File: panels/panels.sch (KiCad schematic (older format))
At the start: 13 parts, among them J1 Barrel_Jack_Switch, J2 Barrel_Jack_Switch, J3 Barrel_Jack_Switch, J4 Barrel_Jack_Switch, J5 XLR3

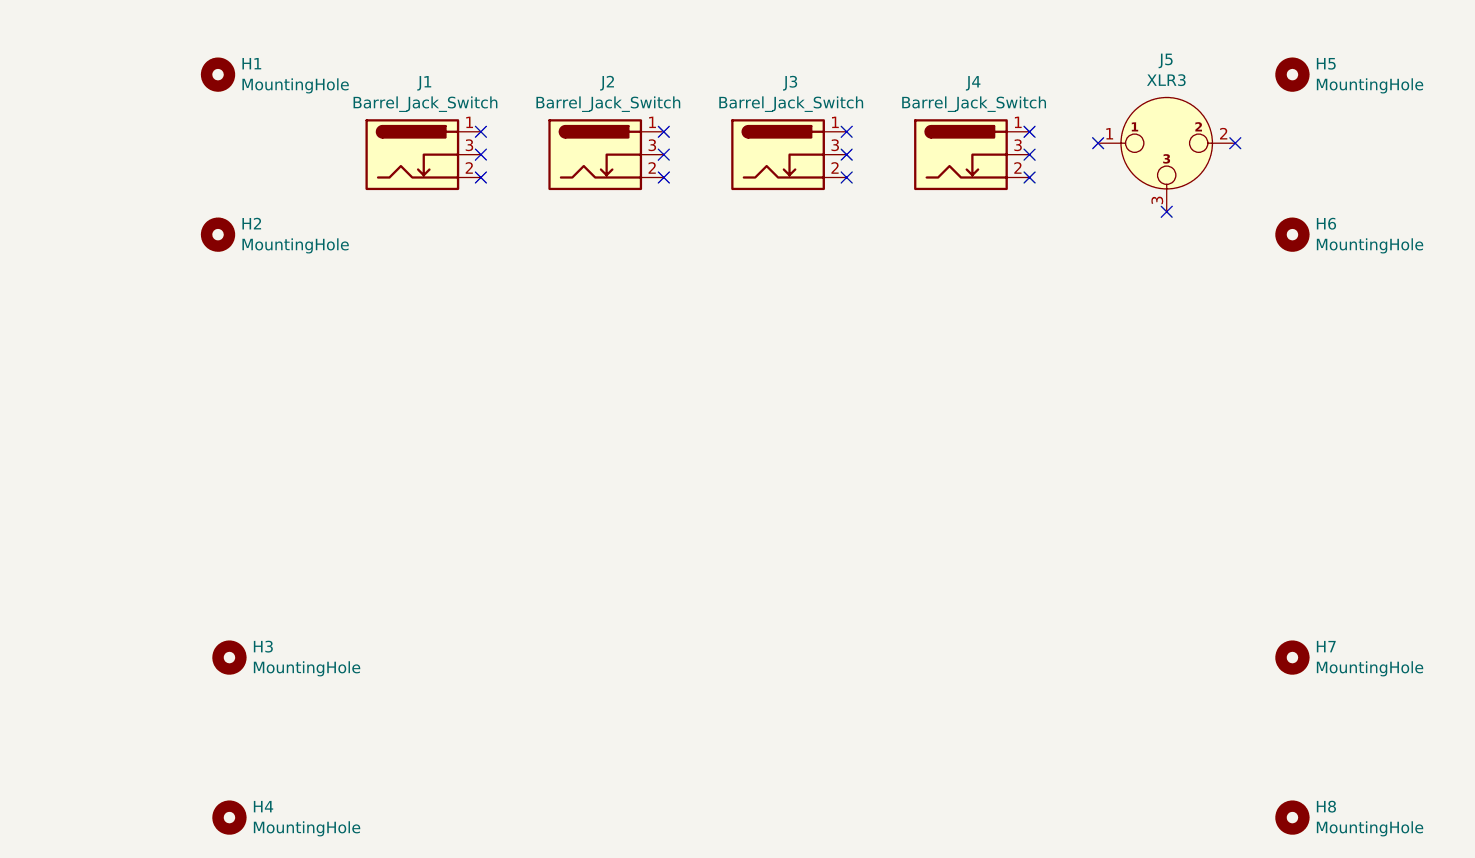
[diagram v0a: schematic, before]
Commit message: Update panels with custom footprints
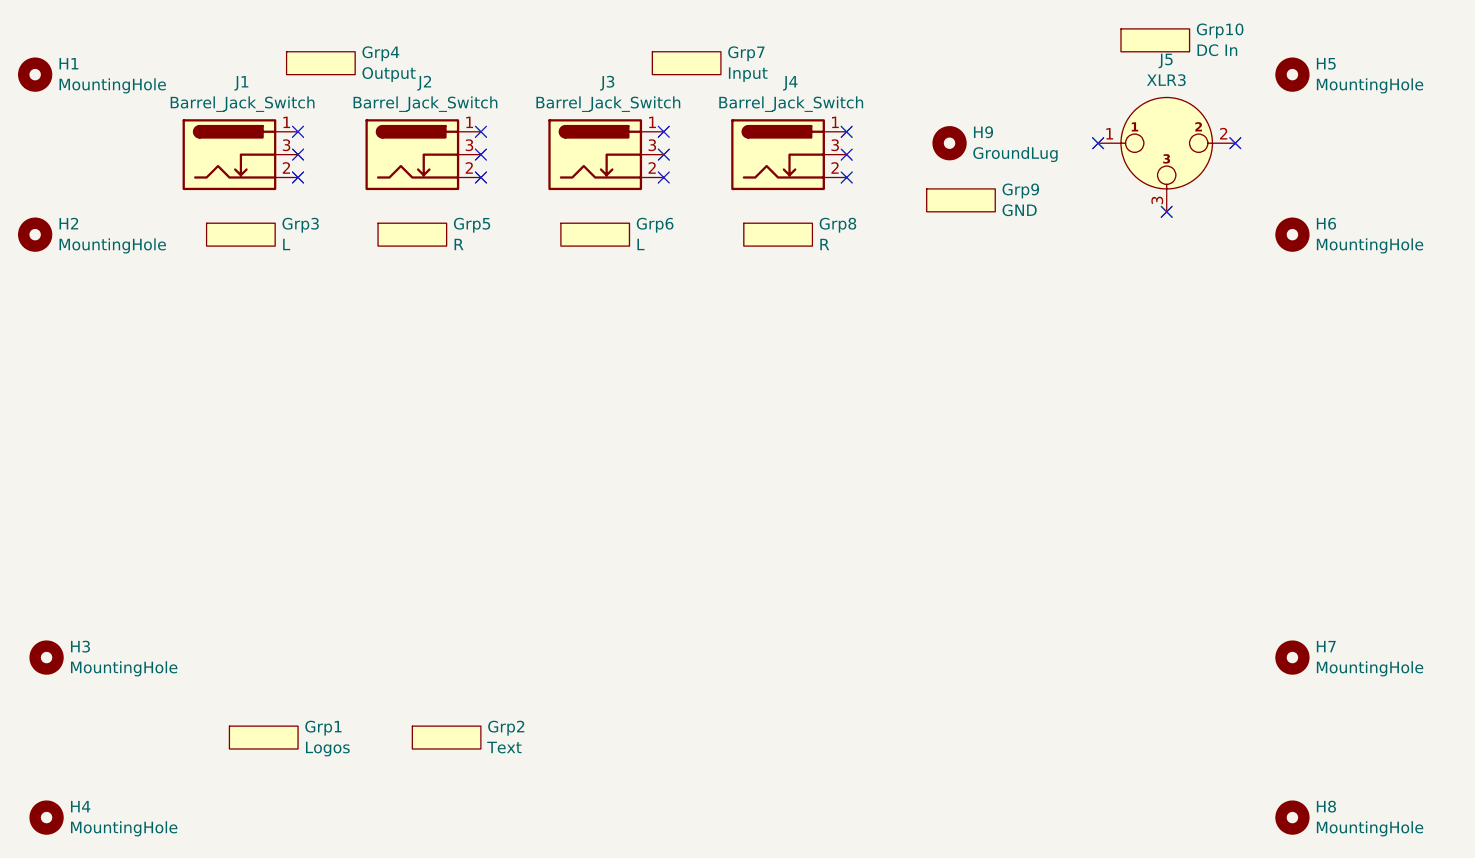
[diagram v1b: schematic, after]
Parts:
- added Grp1: Logos, actidamp-mk4-smd:FP_Logo, symbol actidamp:Graphic
- added Grp10: DC In, actidamp-mk4-smd:BP_text_DC_In, symbol actidamp:Graphic
- added Grp2: Text, actidamp-mk4-smd:FP_text, symbol actidamp:Graphic
- added Grp3, Grp6: L, actidamp-mk4-smd:BP_text_L, symbol actidamp:Graphic
- added Grp4: Output, actidamp-mk4-smd:BP_text_output, symbol actidamp:Graphic
- added Grp5, Grp8: R, actidamp-mk4-smd:BP_text_R, symbol actidamp:Graphic
- added Grp7: Input, actidamp-mk4-smd:BP_text_input, symbol actidamp:Graphic
- added Grp9: GND, actidamp-mk4-smd:BP_text_GND, symbol actidamp:Graphic
- added H9: GroundLug, MountingHole:MountingHole_4.3mm_M4, symbol Mechanical:MountingHole
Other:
- moved on the sheet: H1, H2, H3, H4, J1, J2, J3, J4
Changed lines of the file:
@@
 L Mechanical:MountingHole H1
 U 1 1 5DB88982
-P 2650 1900
-F 0 "H1" H 2750 1946 50  0000 L CNN
-F 1 "MountingHole" H 2750 1855 50  0000 L CNN
-F 2 "MountingHole:MountingHole_3.5mm" H 2650 1900 50  0001 C CNN
-F 3 "~" H 2650 1900 50  0001 C CNN
-	1    2650 1900
+P 1850 1900
+F 0 "H1" H 1950 1946 50  0000 L CNN
+F 1 "MountingHole" H 1950 1855 50  0000 L CNN
+F 2 "MountingHole:MountingHole_3.5mm" H 1850 1900 50  0001 C CNN
+F 3 "~" H 1850 1900 50  0001 C CNN
+	1    1850 1900
 	1    0    0    -1
 $EndComp
@@
 L Mechanical:MountingHole H2
 U 1 1 5DB88E12
-P 2650 2600
-F 0 "H2" H 2750 2646 50  0000 L CNN
-F 1 "MountingHole" H 2750 2555 50  0000 L CNN
-F 2 "MountingHole:MountingHole_3.5mm" H 2650 2600 50  0001 C CNN
-F 3 "~" H 2650 2600 50  0001 C CNN
-	1    2650 2600
+P 1850 2600
+F 0 "H2" H 1950 2646 50  0000 L CNN
+F 1 "MountingHole" H 1950 2555 50  0000 L CNN
+F 2 "MountingHole:MountingHole_3.5mm" H 1850 2600 50  0001 C CNN
+F 3 "~" H 1850 2600 50  0001 C CNN
+	1    1850 2600
 	1    0    0    -1
 $EndComp
@@
 L Mechanical:MountingHole H3
 U 1 1 5DB8B1F4
-P 2700 4450
-F 0 "H3" H 2800 4496 50  0000 L CNN
-F 1 "MountingHole" H 2800 4405 50  0000 L CNN
-F 2 "MountingHole:MountingHole_3.5mm" H 2700 4450 50  0001 C CNN
-F 3 "~" H 2700 4450 50  0001 C CNN
-	1    2700 4450
+P 1900 4450
+F 0 "H3" H 2000 4496 50  0000 L CNN
+F 1 "MountingHole" H 2000 4405 50  0000 L CNN
+F 2 "MountingHole:MountingHole_3.5mm" H 1900 4450 50  0001 C CNN
+F 3 "~" H 1900 4450 50  0001 C CNN
+	1    1900 4450
 	1    0    0    -1
 $EndComp
@@
 L Mechanical:MountingHole H4
 U 1 1 5DB8B208
-P 2700 5150
-F 0 "H4" H 2800 5196 50  0000 L CNN
-F 1 "MountingHole" H 2800 5105 50  0000 L CNN
-F 2 "MountingHole:MountingHole_3.5mm" H 2700 5150 50  0001 C CNN
-F 3 "~" H 2700 5150 50  0001 C CNN
-	1    2700 5150
+P 1900 5150
+F 0 "H4" H 2000 5196 50  0000 L CNN
+F 1 "MountingHole" H 2000 5105 50  0000 L CNN
+F 2 "MountingHole:MountingHole_3.5mm" H 1900 5150 50  0001 C CNN
+F 3 "~" H 1900 5150 50  0001 C CNN
+	1    1900 5150
 	1    0    0    -1
 $EndComp
@@
 L Connector:Barrel_Jack_Switch J1
 U 1 1 5DB95C23
+P 2700 2250
+F 0 "J1" H 2757 2567 50  0000 C CNN
+F 1 "Barrel_Jack_Switch" H 2757 2476 50  0000 C CNN
+F 2 "actidamp-mk4-smd:RCA_x1_PJRAN1X1U_FP" H 2750 2210 50  0001 C CNN
+F 3 "~" H 2750 2210 50  0001 C CNN
+	1    2700 2250
+	1    0    0    -1
+$EndComp
+$Comp
+L Connector:Barrel_Jack_Switch J2
+U 1 1 5DB96D2B
 P 3500 2250
-F 0 "J1" H 3557 2567 50  0000 C CNN
+F 0 "J2" H 3557 2567 50  0000 C CNN
 F 1 "Barrel_Jack_Switch" H 3557 2476 50  0000 C CNN
 F 2 "actidamp-mk4-smd:RCA_x1_PJRAN1X1U_FP" H 3550 2210 50  0001 C CNN
@@
 $EndComp
 $Comp
-L Connector:Barrel_Jack_Switch J2
-U 1 1 5DB96D2B
+L Connector:Barrel_Jack_Switch J3
+U 1 1 5DB97302
 P 4300 2250
-F 0 "J2" H 4357 2567 50  0000 C CNN
+F 0 "J3" H 4357 2567 50  0000 C CNN
 F 1 "Barrel_Jack_Switch" H 4357 2476 50  0000 C CNN
 F 2 "actidamp-mk4-smd:RCA_x1_PJRAN1X1U_FP" H 4350 2210 50  0001 C CNN
@@
 $EndComp
 $Comp
-L Connector:Barrel_Jack_Switch J3
-U 1 1 5DB97302
+L Connector:Barrel_Jack_Switch J4
+U 1 1 5DB977A2
 P 5100 2250
-F 0 "J3" H 5157 2567 50  0000 C CNN
+F 0 "J4" H 5157 2567 50  0000 C CNN
 F 1 "Barrel_Jack_Switch" H 5157 2476 50  0000 C CNN
 F 2 "actidamp-mk4-smd:RCA_x1_PJRAN1X1U_FP" H 5150 2210 50  0001 C CNN
 F 3 "~" H 5150 2210 50  0001 C CNN
 	1    5100 2250
-	1    0    0    -1
-$EndComp
-$Comp
-L Connector:Barrel_Jack_Switch J4
-U 1 1 5DB977A2
-P 5900 2250
-F 0 "J4" H 5957 2567 50  0000 C CNN
-F 1 "Barrel_Jack_Switch" H 5957 2476 50  0000 C CNN
-F 2 "actidamp-mk4-smd:RCA_x1_PJRAN1X1U_FP" H 5950 2210 50  0001 C CNN
-F 3 "~" H 5950 2210 50  0001 C CNN
-	1    5900 2250
 	1    0    0    -1
 $EndComp
@@
 	1    0    0    -1
 $EndComp
+NoConn ~ 3000 2150
+NoConn ~ 3000 2250
+NoConn ~ 3000 2350
 NoConn ~ 3800 2150
 NoConn ~ 3800 2250
@@
 NoConn ~ 5400 2250
 NoConn ~ 5400 2350
-NoConn ~ 6200 2150
-NoConn ~ 6200 2250
-NoConn ~ 6200 2350
 NoConn ~ 6500 2200
 NoConn ~ 6800 2500
 NoConn ~ 7100 2200
+$Comp
+L Mechanical:MountingHole H9
+U 1 1 5DBA5314
+P 5850 2200
+F 0 "H9" H 5950 2246 50  0000 L CNN
+F 1 "GroundLug" H 5950 2155 50  0000 L CNN
+F 2 "MountingHole:MountingHole_4.3mm_M4" H 5850 2200 50  0001 C CNN
+F 3 "~" H 5850 2200 50  0001 C CNN
+	1    5850 2200
+	1    0    0    -1
+$EndComp
+$Comp
+L actidamp:Graphic Grp1
+U 1 1 5DC0A211
+P 2850 4800
+F 0 "Grp1" H 3028 4846 50  0000 L CNN
+F 1 "Logos" H 3028 4755 50  0000 L CNN
+F 2 "actidamp-mk4-smd:FP_Logo" H 2850 4750 50  0001 C CNN
+F 3 "" H 2850 4750 50  0001 C CNN
+	1    2850 4800
+	1    0    0    -1
+$EndComp
+$Comp
+L actidamp:Graphic Grp2
+U 1 1 5DC0A606
+P 3650 4800
+F 0 "Grp2" H 3828 4846 50  0000 L CNN
+F 1 "Text" H 3828 4755 50  0000 L CNN
+F 2 "actidamp-mk4-smd:FP_text" H 3650 4750 50  0001 C CNN
+F 3 "" H 3650 4750 50  0001 C CNN
+	1    3650 4800
+	1    0    0    -1
+$EndComp
+$Comp
+L actidamp:Graphic Grp4
+U 1 1 5DC0FA5B
+P 3100 1850
+F 0 "Grp4" H 3278 1896 50  0000 L CNN
+F 1 "Output" H 3278 1805 50  0000 L CNN
+F 2 "actidamp-mk4-smd:BP_text_output" H 3100 1800 50  0001 C CNN
+F 3 "" H 3100 1800 50  0001 C CNN
+	1    3100 1850
+	1    0    0    -1
+$EndComp
+$Comp
+L actidamp:Graphic Grp7
+U 1 1 5DC0FD71
+P 4700 1850
+F 0 "Grp7" H 4878 1896 50  0000 L CNN
+F 1 "Input" H 4878 1805 50  0000 L CNN
+F 2 "actidamp-mk4-smd:BP_text_input" H 4700 1800 50  0001 C CNN
+F 3 "" H 4700 1800 50  0001 C CNN
+	1    4700 1850
+	1    0    0    -1
+$EndComp
+$Comp
+L actidamp:Graphic Grp3
+U 1 1 5DC10052
+P 2750 2600
+F 0 "Grp3" H 2928 2646 50  0000 L CNN
+F 1 "L" H 2928 2555 50  0000 L CNN
+F 2 "actidamp-mk4-smd:BP_text_L" H 2750 2550 50  0001 C CNN
+F 3 "" H 2750 2550 50  0001 C CNN
+	1    2750 2600
+	1    0    0    -1
+$EndComp
+$Comp
+L actidamp:Graphic Grp5
+U 1 1 5DC10302
+P 3500 2600
+F 0 "Grp5" H 3678 2646 50  0000 L CNN
+F 1 "R" H 3678 2555 50  0000 L CNN
+F 2 "actidamp-mk4-smd:BP_text_R" H 3500 2550 50  0001 C CNN
+F 3 "" H 3500 2550 50  0001 C CNN
+	1    3500 2600
+	1    0    0    -1
+$EndComp
+$Comp
+L actidamp:Graphic Grp6
+U 1 1 5DC1052B
+P 4300 2600
+F 0 "Grp6" H 4478 2646 50  0000 L CNN
+F 1 "L" H 4478 2555 50  0000 L CNN
+F 2 "actidamp-mk4-smd:BP_text_L" H 4300 2550 50  0001 C CNN
+F 3 "" H 4300 2550 50  0001 C CNN
+	1    4300 2600
+	1    0    0    -1
+$EndComp
+$Comp
+L actidamp:Graphic Grp8
+U 1 1 5DC10681
+P 5100 2600
+F 0 "Grp8" H 5278 2646 50  0000 L CNN
+F 1 "R" H 5278 2555 50  0000 L CNN
+F 2 "actidamp-mk4-smd:BP_text_R" H 5100 2550 50  0001 C CNN
+F 3 "" H 5100 2550 50  0001 C CNN
+	1    5100 2600
+	1    0    0    -1
+$EndComp
+$Comp
+L actidamp:Graphic Grp10
+U 1 1 5DC10B64
+P 6750 1750
+F 0 "Grp10" H 6928 1796 50  0000 L CNN
+F 1 "DC In" H 6928 1705 50  0000 L CNN
+F 2 "actidamp-mk4-smd:BP_text_DC_In" H 6750 1700 50  0001 C CNN
+F 3 "" H 6750 1700 50  0001 C CNN
+	1    6750 1750
+	1    0    0    -1
+$EndComp
+$Comp
+L actidamp:Graphic Grp9
+U 1 1 5DC1096B
+P 5900 2450
+F 0 "Grp9" H 6078 2496 50  0000 L CNN
+F 1 "GND" H 6078 2405 50  0000 L CNN
+F 2 "actidamp-mk4-smd:BP_text_GND" H 5900 2400 50  0001 C CNN
+F 3 "" H 5900 2400 50  0001 C CNN
+	1    5900 2450
+	1    0    0    -1
+$EndComp
 $EndSCHEMATC
